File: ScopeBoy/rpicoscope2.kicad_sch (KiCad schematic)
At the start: 79 parts, among them J1 Conn_01x02, J2 Conn_01x02_Male, J3 Conn_01x05, J4 Conn_01x10, J5 Conn_01x04, U1 LP2985-3.3, U10 LM4040DBZ-2.0, U11 TLV3501, U12 DAC5571, U13 TLV271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

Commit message: Initial version of the PCB done
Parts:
- added J6, J7: Conn_01x03, Connector_JST:JST_SH_SM03B-SRSS-TB_1x03-1MP_P1.00mm_Horizontal, symbol Connector_Generic:Conn_01x03
- added J8: Conn_01x02, Connector_JST:JST_PH_S2B-PH-SM4-TB_1x02-1MP_P2.00mm_Horizontal, symbol Connector_Generic:Conn_01x02
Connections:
- net SEL is gone; now on net ROTSW: U9.32 (GP27)
- net +5V: now also J8.1 (Pin_1)
- net GND: now also J6.2 (Pin_2), J7.2 (Pin_2), J8.2 (Pin_2)
- net ROTSW: no longer U9.15 (GP11)
- net SEL0: now also U9.14 (GP10); no longer U9.11 (GP8)
- net SEL1: now also U9.15 (GP11); no longer U9.12 (GP9)
- net SWCLK: now reaches U9.41 (SWCLK)
- net SWCLK: now also J7.1 (Pin_1)
- net SWIO: now reaches U9.43 (SWIO)
- net SWIO: now also J7.3 (Pin_3)
- new net RX: J6.1 (Pin_1), U9.12 (GP9)
- new net TX: J6.3 (Pin_3), U9.11 (GP8)
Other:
- note added: "Debug"
- note added: "Debug Connectors"
- note added: "Power Connector"
- note added: "UART"

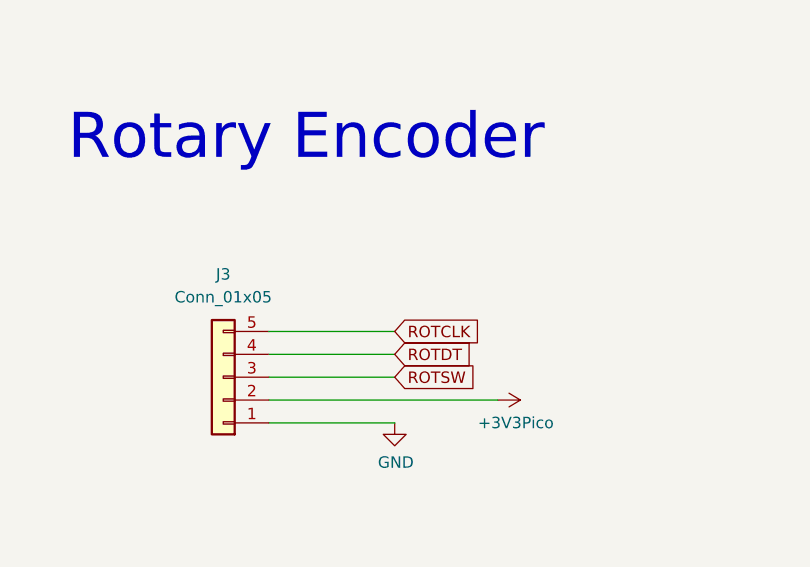
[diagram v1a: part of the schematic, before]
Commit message: Added caps on encoder
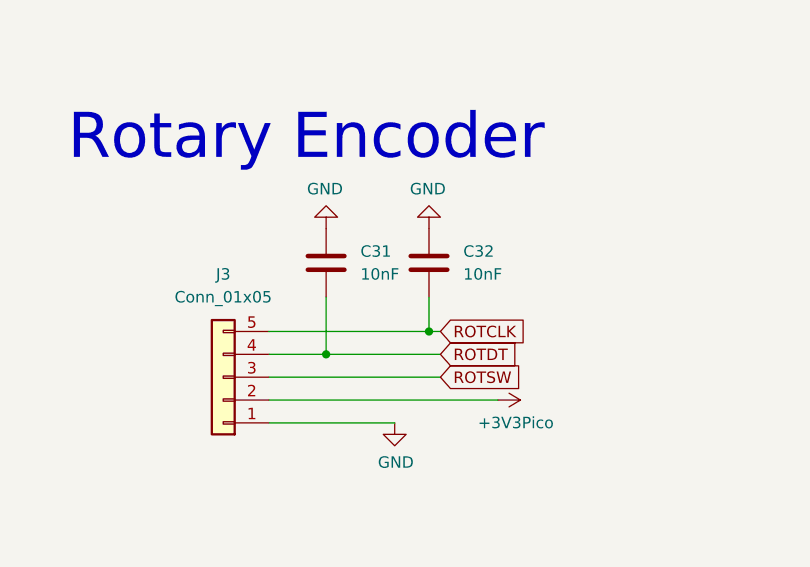
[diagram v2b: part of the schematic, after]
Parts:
- added C31, C32: 10nF, Capacitor_SMD:C_0603_1608Metric, symbol Device:C
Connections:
- net GND: now also C31.1, C32.1
- net ROTCLK: now also C32.2
- net ROTDT: now also C31.2

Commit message: Final revision of PCB. Updated some components
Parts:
- added Q1: DMG2305UX-7, Package_TO_SOT_SMD:SOT-23-3, symbol Device:Q_PMOS_GSD
- C31, C32: LCSC Part # (none) -> C1589; MFR. Part # (none) -> CL10B103KB8NNNC
- C7: LCSC Part # C23969 -> C277513; MFR. Part # CL10C010CB8NNNC -> CC0603CRNPO9BN1R0
- C9: LCSC Part # C1679 -> C318672; MFR. Part # 0603CG6R8C500NT -> CL10C6R8CB8NNNC
- J5: value Conn_01x04 -> SM04B-SRSS-TB; LCSC Part # (none) -> C160404; MFR. Part # (none) -> SM04B-SRSS-TB(LF)(SN)
- J6, J7: value Conn_01x03 -> SM03B-SRSS-TB; LCSC Part # (none) -> C160403; MFR. Part # (none) -> SM03B-SRSS-TB(LF)(SN)
- J8: footprint Connector_JST:JST_PH_S2B-PH-SM4-TB_1x02-1MP_P2.00mm_Horizontal -> Connector_PinHeader_2.54mm:PinHeader_1x02_P2.54mm_Vertical
- R22: LCSC Part # C23345 -> C193390; MFR. Part # 0603WAF220JT5E -> ERJ3EKF1004V
- U3: value TPH2501 -> OPA354; LCSC Part # C139385 -> C36384; MFR. Part # (none) -> OPA354AIDBVR
- U6: LCSC Part # C181539 -> C2058414; MRF. Part # (none) -> OPA830IDBVR
- U9: LCSC Part # (none) -> C7203002; MFR. Part # (none) -> SC0915
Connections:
- net VSYS: now reaches U9.39 (VSYS)
- net VSYS: now also C1.1, C2.2, U1.1 (VIN), U1.3 (ON/~{OFF}), U2.12 (EN+), U2.3 (VIN), U2.8 (EN-), Q1.2 (S)
- removed net +5V: C1.1, C2.2, J8.1 (Pin_1), U1.1 (VIN), U1.3 (ON/~{OFF}), U2.12 (EN+), U2.3 (VIN), U2.8 (EN-), U9.40 (VUSB)
- new net: J8.1 (Pin_1), Q1.3 (D)
- new net VBUS: Q1.1 (G), U9.40 (VUSB)
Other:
- note removed: "OPA357"
